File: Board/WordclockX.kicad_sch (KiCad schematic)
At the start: 86 parts, among them J1 USB_C_Receptacle_USB2.0, SW1 SW_Push_Dual, SW2 SW_Push_Dual, U1 MIC5504-3.3YM5, U2 W25Q16JLSNIG, U3 RP2040, U4 MCP7940N-xST, U5 74HCT137, U6 PCA9626, U7 PCA9626, Y1 12M, Y2 32768

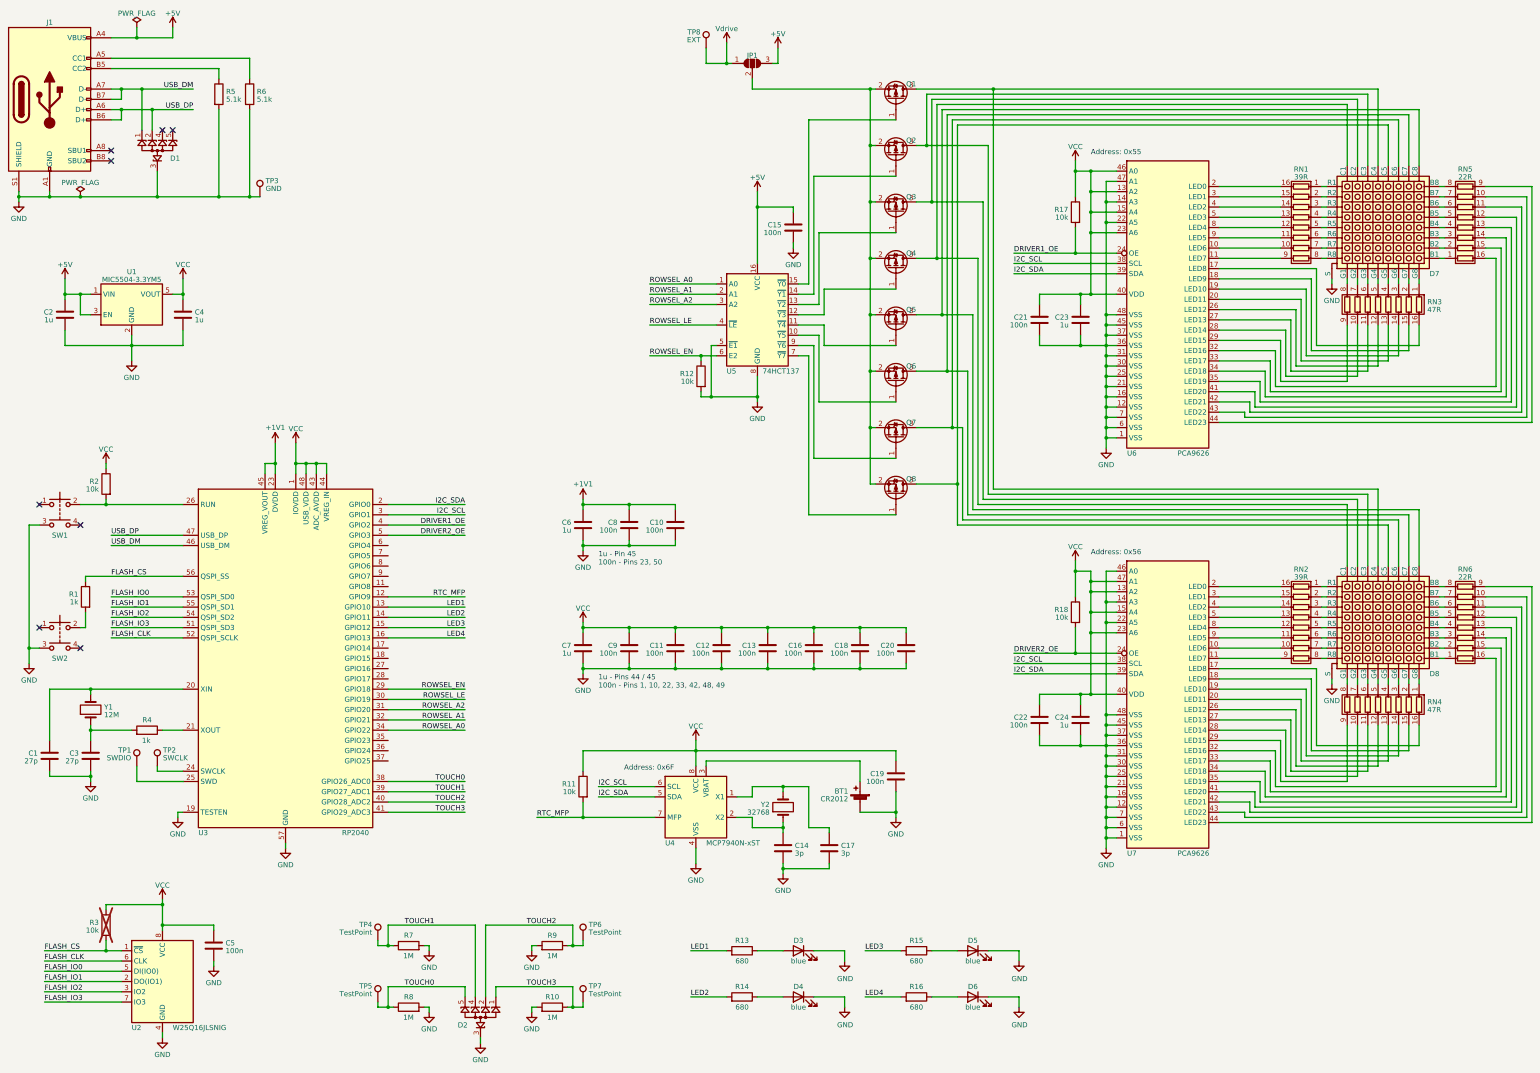
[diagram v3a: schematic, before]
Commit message: Most of the routing done, I2C pullups missing!
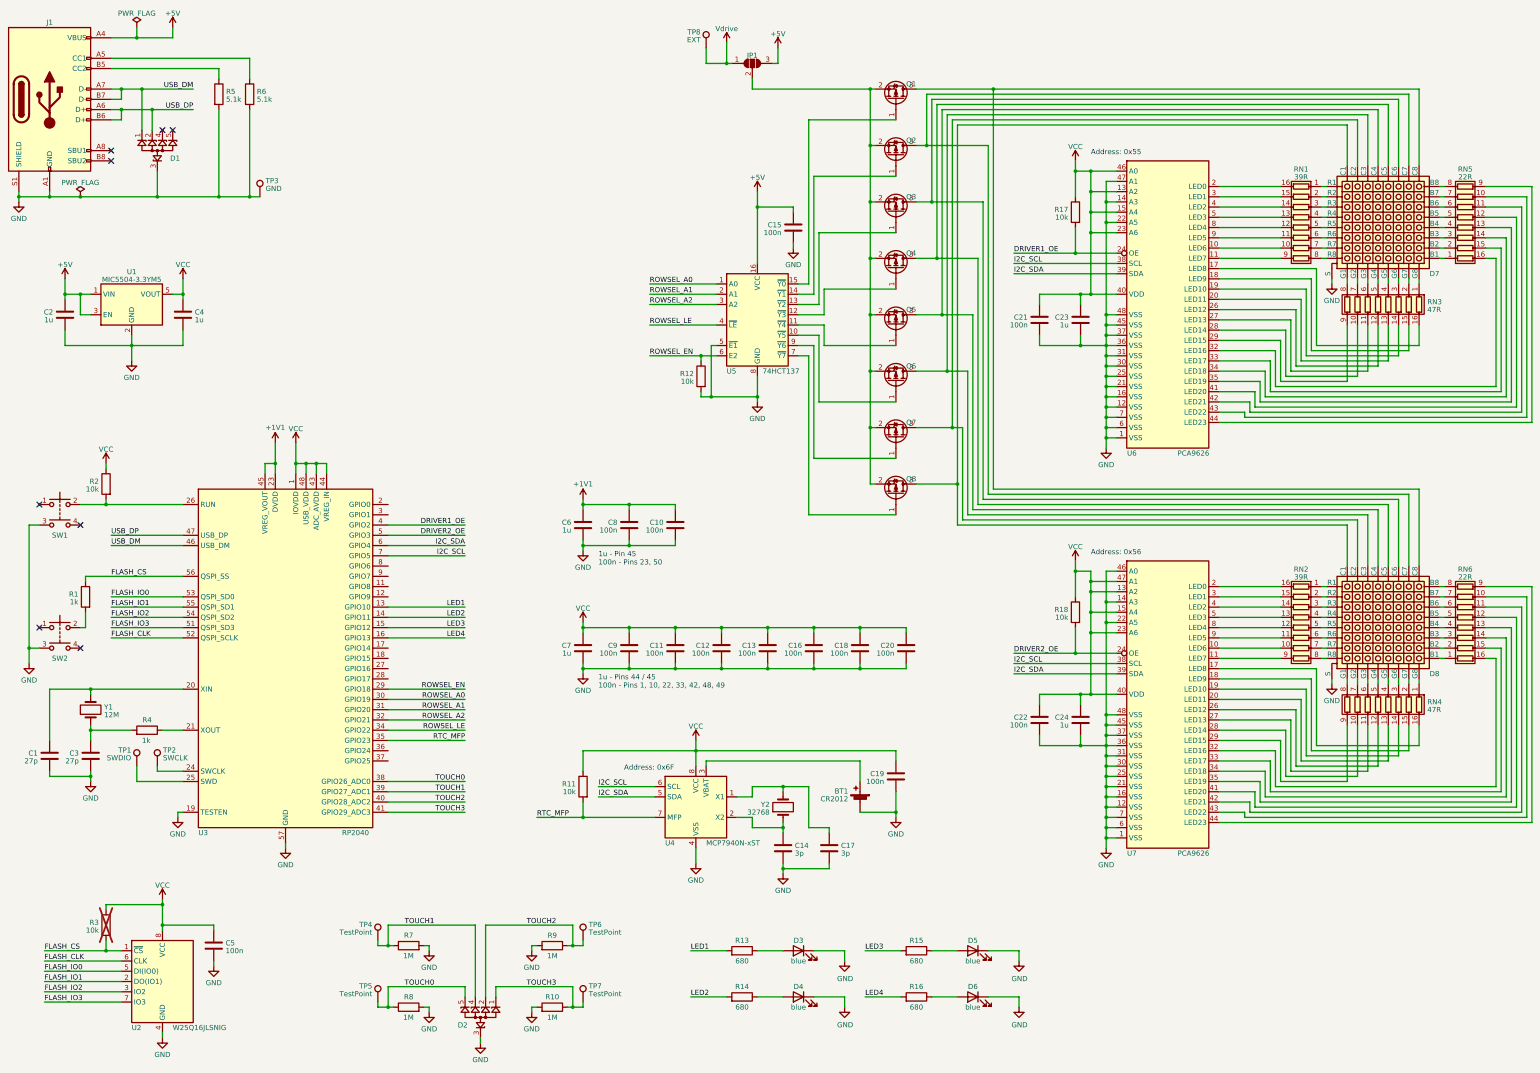
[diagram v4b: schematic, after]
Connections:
- net I2C_SCL: now also U3.7 (GPIO5); no longer U3.3 (GPIO1)
- net I2C_SDA: now also U3.6 (GPIO4); no longer U3.2 (GPIO0)
- net ROWSEL_A0: now also U3.30 (GPIO19); no longer U3.34 (GPIO22)
- net ROWSEL_A1: now also U3.31 (GPIO20); no longer U3.32 (GPIO21)
- net ROWSEL_A2: now also U3.32 (GPIO21); no longer U3.31 (GPIO20)
- net ROWSEL_LE: now also U3.34 (GPIO22); no longer U3.30 (GPIO19)
- net RTC_MFP: now also U3.35 (GPIO23); no longer U3.12 (GPIO9)
- net at D7.32 (C8), D8.32 (C8): now also Q1.3 (D); no longer Q5.3 (D)
- net at D7.19 (C3), D8.19 (C3): now also Q6.3 (D); no longer Q2.3 (D)
- net at D7.20 (C4), D8.20 (C4): now also Q5.3 (D); no longer Q1.3 (D)
- net at D7.17 (C1), D8.17 (C1): now also Q8.3 (D); no longer Q4.3 (D)
- net at D7.18 (C2), D8.18 (C2): now also Q7.3 (D); no longer Q3.3 (D)
- net at D7.29 (C5), D8.29 (C5): now also Q4.3 (D); no longer Q8.3 (D)
- net at D7.30 (C6), D8.30 (C6): now also Q3.3 (D); no longer Q7.3 (D)
- net at D7.31 (C7), D8.31 (C7): now also Q2.3 (D); no longer Q6.3 (D)

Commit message: Routing almost done. Only touch buttons and battery supply missing.
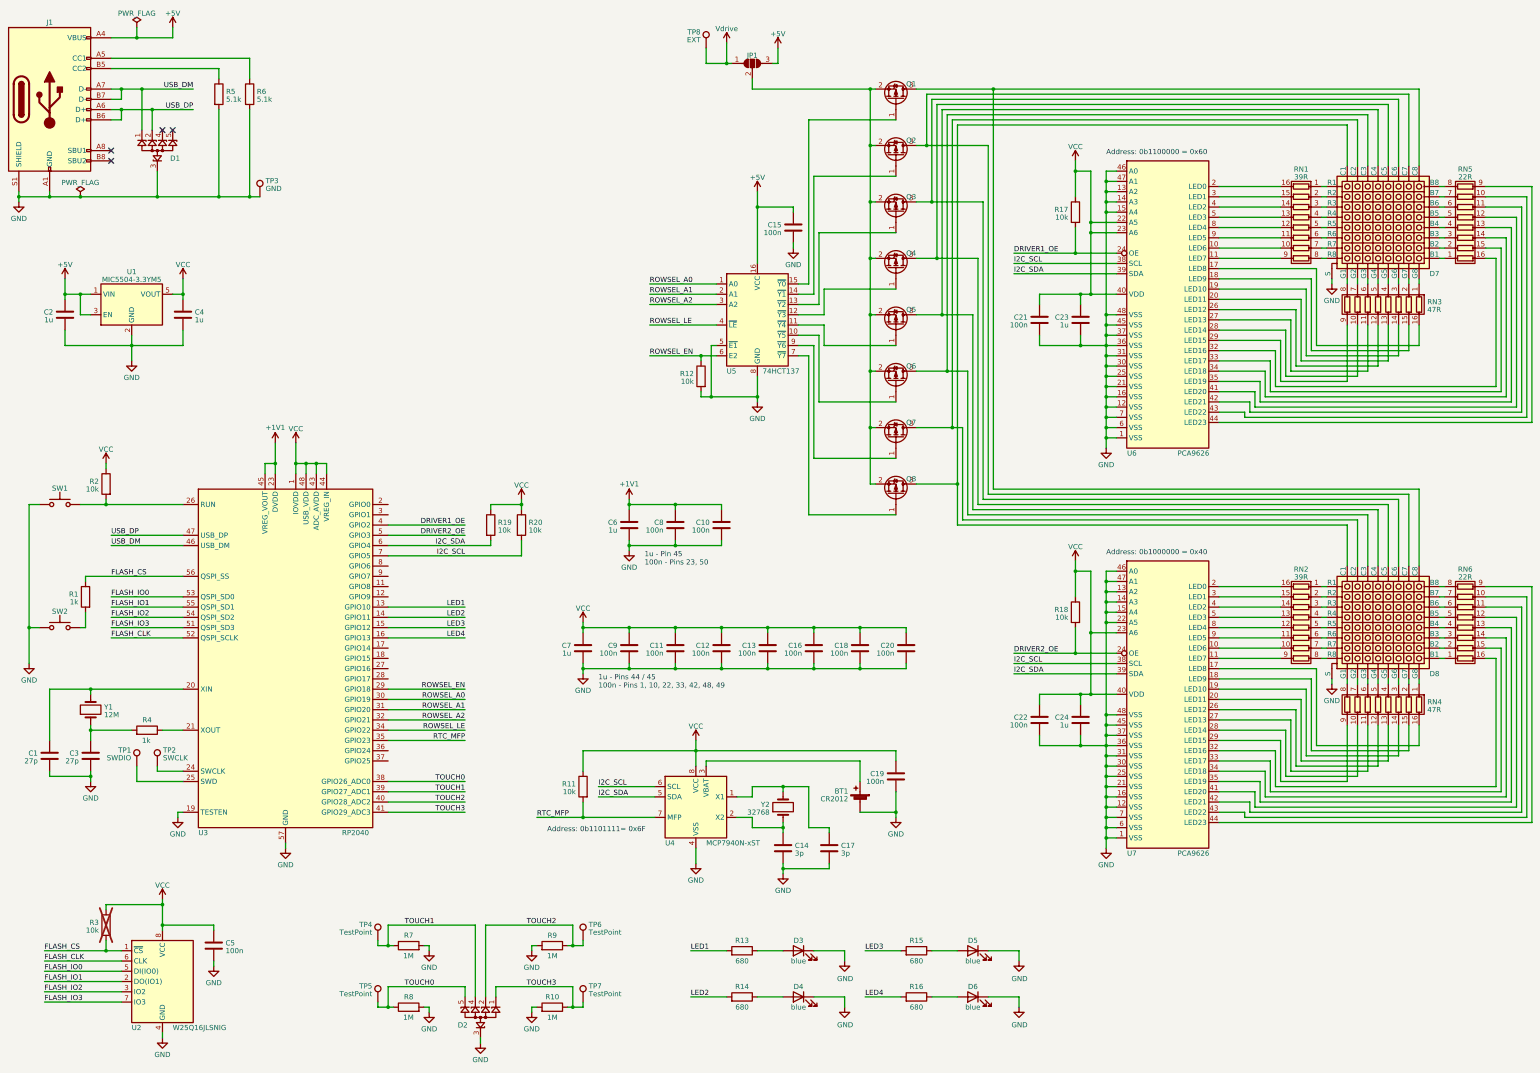
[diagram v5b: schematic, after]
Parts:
- added R19, R20: 10k, Resistor_SMD:R_0603_1608Metric, symbol Device:R
- SW1, SW2: symbol Switch:SW_Push_Dual -> Switch:SW_Push
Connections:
- net GND: now also SW1.1, SW2.1, U6.13 (A2), U6.15 (A4), U6.46 (A0), U7.13 (A2), U7.15 (A4), U7.47 (A1); no longer SW1.3, SW2.3, U6.22 (A5)
- net I2C_SCL: now also R20.2
- net I2C_SDA: now also R19.2
- net VCC: now also U6.22 (A5), R19.1, R20.1; no longer U6.13 (A2), U6.15 (A4), U6.46 (A0), U7.13 (A2), U7.15 (A4), U7.47 (A1)
- no-connect marks 8 -> 4
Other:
- note added: "Address: 0b1000000 = 0x40"
- note added: "Address: 0b1100000 = 0x60"
- note added: "Address: 0b1101111= 0x6F"
- note removed: "Address: 0x55"
- note removed: "Address: 0x56"
- note removed: "Address: 0x6F"
- moved on the sheet: C10, C6, C8

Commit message: All routing done
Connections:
- net TOUCH1: now also R9.1, TP6.1; no longer R7.1, TP4.1
- net TOUCH2: now also R7.1, TP4.1; no longer R9.1, TP6.1
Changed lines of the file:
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@@
-    (stroke (width 0) (type default))
-  )
-  (wire (pts (xy 138.43 242.57) (xy 160.02 242.57))
     (stroke (width 0) (type default))
   )
@@
     (stroke (width 0) (type default))
   )
+  (wire (pts (xy 137.16 251.46) (xy 137.16 242.57))
+    (stroke (width 0) (type default))
+  )
   (wire (pts (xy 342.9 82.55) (xy 320.04 82.55))
     (stroke (width 0) (type default))
@@
     (stroke (width 0) (type default))
   )
+  (wire (pts (xy 138.43 250.19) (xy 135.89 250.19))
+    (stroke (width 0) (type default))
+  )
   (wire (pts (xy 264.16 35.56) (xy 369.57 35.56))
     (stroke (width 0) (type default))
@@
     (stroke (width 0) (type default))
   )
+  (wire (pts (xy 135.89 250.19) (xy 135.89 242.57))
+    (stroke (width 0) (type default))
+  )
   (wire (pts (xy 336.55 95.25) (xy 320.04 95.25))
     (stroke (width 0) (type default))
@@
     (stroke (width 0) (type default))
   )
-  (wire (pts (xy 138.43 242.57) (xy 138.43 260.35))
-    (stroke (width 0) (type default))
-  )
   (wire (pts (xy 339.09 104.14) (xy 359.41 104.14))
     (stroke (width 0) (type default))
@@
     (stroke (width 0) (type default))
   )
+  (wire (pts (xy 135.89 251.46) (xy 135.89 260.35))
+    (stroke (width 0) (type default))
+  )
   (wire (pts (xy 369.57 82.55) (xy 369.57 83.82))
     (stroke (width 0) (type default))
@@
     (stroke (width 0) (type default))
   )
+  (wire (pts (xy 138.43 260.35) (xy 138.43 250.19))
+    (stroke (width 0) (type default))
+  )
   (wire (pts (xy 320.04 77.47) (xy 335.28 77.47))
     (stroke (width 0) (type default))
@@
     (stroke (width 0) (type default))
   )
-  (wire (pts (xy 135.89 242.57) (xy 135.89 260.35))
-    (stroke (width 0) (type default))
-  )
   (wire (pts (xy 222.25 91.44) (xy 222.25 85.09))
     (stroke (width 0) (type default))
@@
     (stroke (width 0) (type default))
   )
+  (wire (pts (xy 137.16 242.57) (xy 160.02 242.57))
+    (stroke (width 0) (type default))
+  )
   (wire (pts (xy 198.12 24.13) (xy 198.12 29.21))
     (stroke (width 0) (type default))
@@
   )
   (wire (pts (xy 345.44 163.83) (xy 346.71 163.83))
+    (stroke (width 0) (type default))
+  )
+  (wire (pts (xy 137.16 251.46) (xy 135.89 251.46))
     (stroke (width 0) (type default))
   )
@@
     (effects (font (size 1.27 1.27)) (justify left bottom))
   )
-  (label "TOUCH2" (at 148.59 242.57 0) (fields_autoplaced)
+  (label "TOUCH2" (at 118.11 242.57 0) (fields_autoplaced)
     (effects (font (size 1.27 1.27)) (justify left bottom))
   )
@@
     (effects (font (size 1.27 1.27)) (justify right bottom))
   )
-  (label "TOUCH1" (at 125.73 242.57 180) (fields_autoplaced)
+  (label "TOUCH1" (at 156.21 242.57 180) (fields_autoplaced)
     (effects (font (size 1.27 1.27)) (justify right bottom))
   )

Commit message: Finished board for production
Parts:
- added TP10: BCKP2, TestPoint:TestPoint_Pad_1.0x1.0mm, symbol Connector:TestPoint
- added TP9: BCKP1, TestPoint:TestPoint_Pad_1.0x1.0mm, symbol Connector:TestPoint
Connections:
- net BACKUP1: now reaches U3.11 (GPIO8)
- net BACKUP1: now also TP9.1
- net BACKUP2: now reaches U3.12 (GPIO9)
- net BACKUP2: now also TP10.1
- net Vdrive: no longer names the net of JP1.1 (A), TP8.1
- no-connect marks 4 -> 14
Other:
- note added: "Address: 0b1101111 = 0x6F"
- note removed: "Address: 0b1101111= 0x6F"
- moved on the sheet: BT1, TP8
